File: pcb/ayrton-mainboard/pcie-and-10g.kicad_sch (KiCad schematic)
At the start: 1 part, among them U1 STM32MP257FAI3

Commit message: Continued initial system design
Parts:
- added C119, C120, C121, C122, C123, C124: 0.1 uF, symbol device:C
- added C125, C126, C129, C130: 0.1 uF, azonenberg_pcb:EIA_0402_CAP_NOSILK, symbol device:C
- added C127, C128: 22 uF, azonenberg_pcb:EIA_1206_CAP_NOSILK, symbol device:C
- added J4: CONN_SFP_HOST, azonenberg_pcb:CONN_SFP+_AMPHENOL_UE76_A10_2000T, symbol special-azonenberg:CONN_SFP_HOST
- added J5: SFP_CAGE, azonenberg_pcb:CONN_SFP_CAGE_TE_2007194-1, symbol Connector:Conn_01x01
- added L1, L2: 4.7 uH, azonenberg_pcb:EIA_0805_INDUCTOR_NOSILK, symbol passive-azonenberg:INDUCTOR_PWROUT
- added R26, R27, R28, R29: 4.7K, azonenberg_pcb:EIA_0402_RES_NOSILK, symbol device:R
- added R30: 10K, azonenberg_pcb:EIA_0402_RES_NOSILK, symbol device:R
- added R31: 0.1, azonenberg_pcb:EIA_0402_RES_NOSILK, symbol device:R
- added R32, R33: 0.5, azonenberg_pcb:EIA_0402_RES_NOSILK, symbol device:R
- added R34: 200, symbol device:R
- added U2: XC7K160T-2FFG676C, symbol xilinx-azonenberg:XC7KxT-FFG676
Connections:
- net SOC_PCIE_CLKIN_N: now reaches U1.AA18 (PCIE_CLKINN)
- net SOC_PCIE_TX_P: now reaches U1.AA19 (COMBOPHY_TX1P)
- net SOC_PCIE_TX_P: now also C119.2
- net SOC_PCIE_RX_P: now reaches U1.AA20 (COMBOPHY_RX1P)
- net SOC_PCIE_RX_P: now also C121.2
- net SOC_PCIE_CLKOUT_P: now reaches U1.AA21 (PCIE_CLKOUTP)
- net SOC_PCIE_CLKOUT_P: now also C123.2
- net SOC_PCIE_TX_N: now reaches U1.AB19 (COMBOPHY_TX1N)
- net SOC_PCIE_TX_N: now also C120.2
- net SOC_PCIE_RX_N: now reaches U1.AB20 (COMBOPHY_RX1N)
- net SOC_PCIE_RX_N: now also C122.2
- net SOC_PCIE_CLKOUT_N: now reaches U1.AB21 (PCIE_CLKOUTN)
- net SOC_PCIE_CLKOUT_N: now also C124.1
- net SOC_PCIE_CLKIN_P: now reaches U1.Y18 (PCIE_CLKINP)
- net at U1.Y20 (COMBOPHY_REXT): now also R34.2
- new net: C125.1, C126.1, L1.2, L2.2, R31.1
- new net: C128.2, R33.2
- new net: C127.2, R32.2
- new net 3V3: R26.1, R27.1, R28.1, R29.1, R30.1, R31.2
- new net FPGA_PCIE_RX_N: C120.1, U2.R3 (MGTXRXN0_115)
- new net FPGA_PCIE_RX_P: C119.1, U2.R4 (MGTXRXP0_115)
- new net FPGA_PCIE_TX_N: C122.1, U2.P1 (MGTXTXN0_115)
- new net FPGA_PCIE_TX_P: C121.1, U2.P2 (MGTXTXP0_115)
- new net GND: C125.2, C126.2, C129.2, C130.2, J4.1 (GND_TX), J4.10 (GND_RX), J4.11 (GND_RX), J4.14 (GND_RX), J4.17 (GND_TX), J4.20 (GND_TX), J5.1 (Pin_1), R32.1, R33.1, R34.1
- new net GTX_REFCLK_156M25_N: U2.H5 (MGTREFCLK0N_115)
- new net GTX_REFCLK_156M25_P: U2.H6 (MGTREFCLK0P_115)
- new net GTX_REFCLK_PCIE_N: C124.2, U2.K5 (MGTREFCLK1N_115)
- new net GTX_REFCLK_PCIE_P: C123.1, U2.K6 (MGTREFCLK1P_115)
- new net SFP_I2C_SCL: J4.5 (SCL), R26.2
- new net SFP_I2C_SDA: J4.4 (SDA), R27.2
- new net SFP_MOD_ABS: J4.6 (MOD_ABS), R30.2
- new net SFP_RS0: J4.7 (RS0)
- new net SFP_RS1: J4.9 (RS1)
- new net SFP_RX_LOS: J4.8 (RX_LOS), R29.2
- new net SFP_RX_N: J4.12 (RX_N), U2.N3 (MGTXRXN1_115)
- new net SFP_RX_P: J4.13 (RX_P), U2.N4 (MGTXRXP1_115)
- new net SFP_TX_DISABLE: J4.3 (TX_DISABLE)
- new net SFP_TX_FAULT: J4.2 (TX_FAULT), R28.2
- new net SFP_TX_N: J4.19 (TX_N), U2.M1 (MGTXTXN1_115)
- new net SFP_TX_P: J4.18 (TX_P), U2.M2 (MGTXTXP1_115)
- new net SFP_VDD_RX: C127.1, C129.1, J4.15 (VDD_RX), L1.1
- new net SFP_VDD_TX: C128.1, C130.1, J4.16 (VDD_TX), L2.1
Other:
- note added: "SFP pullup/downs"
- moved on the sheet: U1J

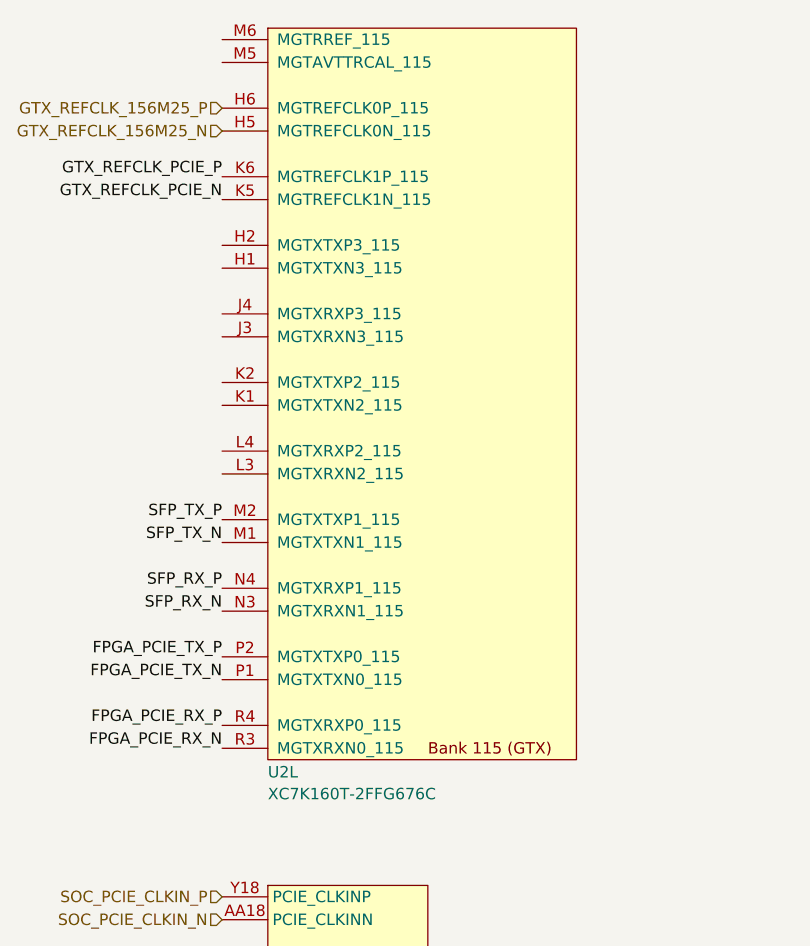
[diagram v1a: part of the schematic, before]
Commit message: Continued initial schematic, working on LPDDR4
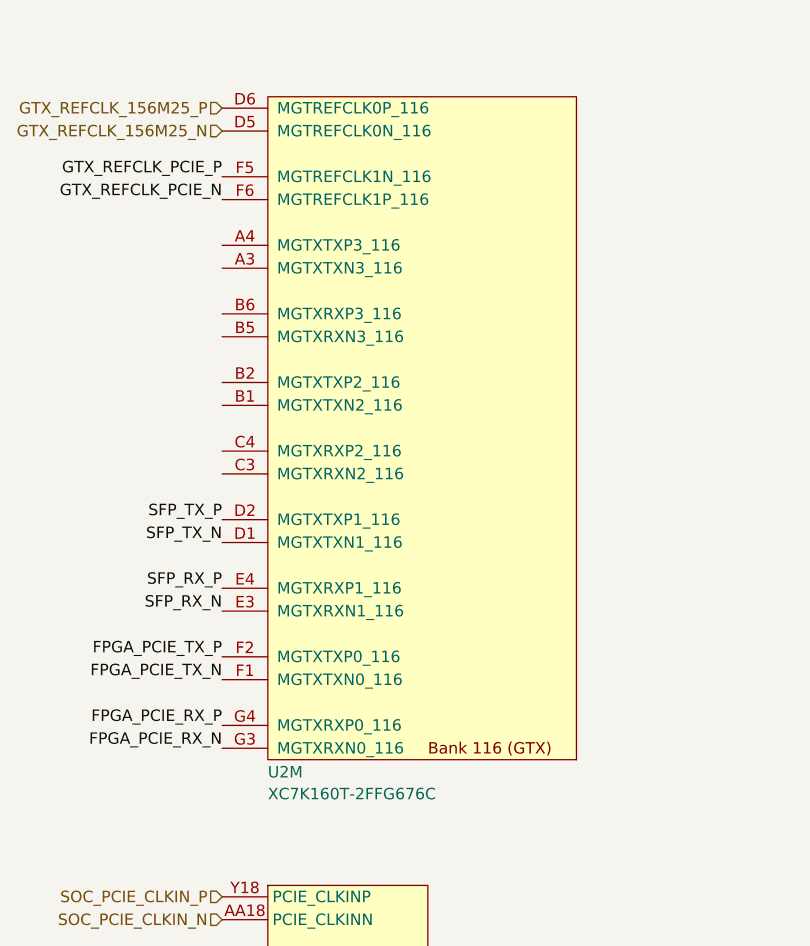
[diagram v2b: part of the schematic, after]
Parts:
- removed U2: XC7K160T-2FFG676C, symbol xilinx-azonenberg:XC7KxT-FFG676
- added U2: XC7K160T-2FFG676C, symbol xilinx-azonenberg:XC7KxT-FFG676
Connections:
- net FPGA_PCIE_RX_N: now also U2.G3 (MGTXRXN0_116)
- net FPGA_PCIE_RX_P: now also U2.G4 (MGTXRXP0_116)
- net FPGA_PCIE_TX_N: now also U2.F1 (MGTXTXN0_116)
- net FPGA_PCIE_TX_P: now also U2.F2 (MGTXTXP0_116)
- net GTX_REFCLK_156M25_N: now also U2.D5 (MGTREFCLK0N_116)
- net GTX_REFCLK_156M25_P: now also U2.D6 (MGTREFCLK0P_116)
- net GTX_REFCLK_PCIE_N: now also U2.F6 (MGTREFCLK1P_116)
- net GTX_REFCLK_PCIE_P: now also U2.F5 (MGTREFCLK1N_116)
- net SFP_RX_N: now also U2.E3 (MGTXRXN1_116)
- net SFP_RX_P: now also U2.E4 (MGTXRXP1_116)
- net SFP_TX_N: now also U2.D1 (MGTXTXN1_116)
- net SFP_TX_P: now also U2.D2 (MGTXTXP1_116)
